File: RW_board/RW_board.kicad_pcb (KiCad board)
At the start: 4 copper layers, 45.6 x 45.6 mm, 129 parts, among them IC201 MAX44284WAUT+T, IC301 MCT8316Z0RQRGFRQ1, J1 Conn_01x08_Pin, J2 1-84953-1, J401 USB4105-GF-A, J402 20021521-00010T4LF, Q201 BSZ300N15NS5ATMA1, SW401 SW_Push, U201 LM5022MM, U401 ATSAMD21G18A-M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

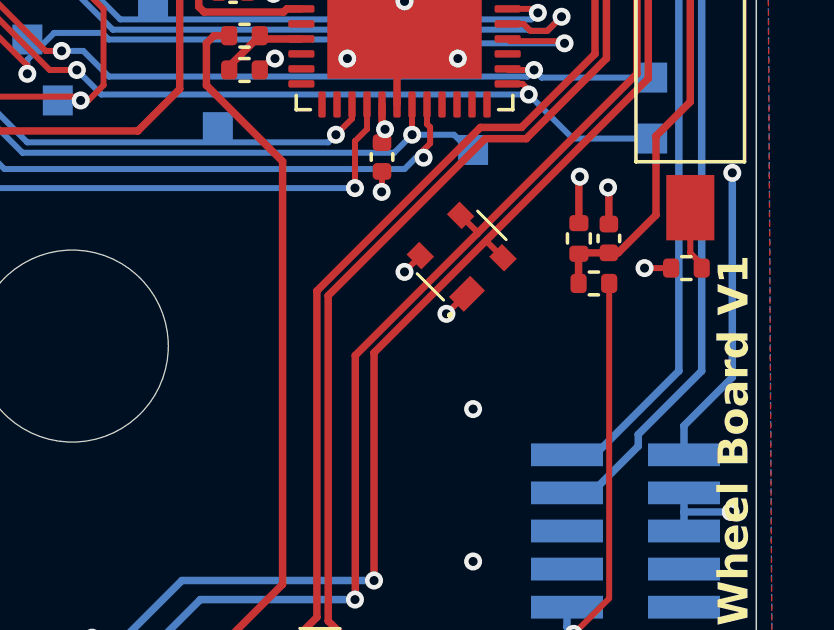
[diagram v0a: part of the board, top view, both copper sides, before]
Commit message: Updated logo silkscreen, generated production files
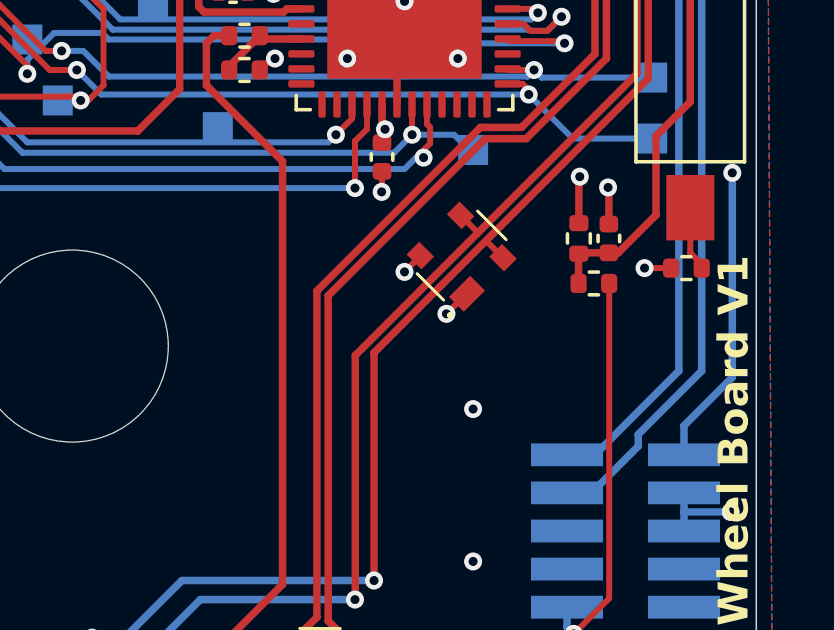
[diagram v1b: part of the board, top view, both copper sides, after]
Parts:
- removed the G*** at (157.9, 104.2)
- added G***: LOGO, LOGO, B.Cu at (154.5, 104.6)
